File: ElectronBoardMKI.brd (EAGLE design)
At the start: 95.9 x 82.6 mm, 22 parts

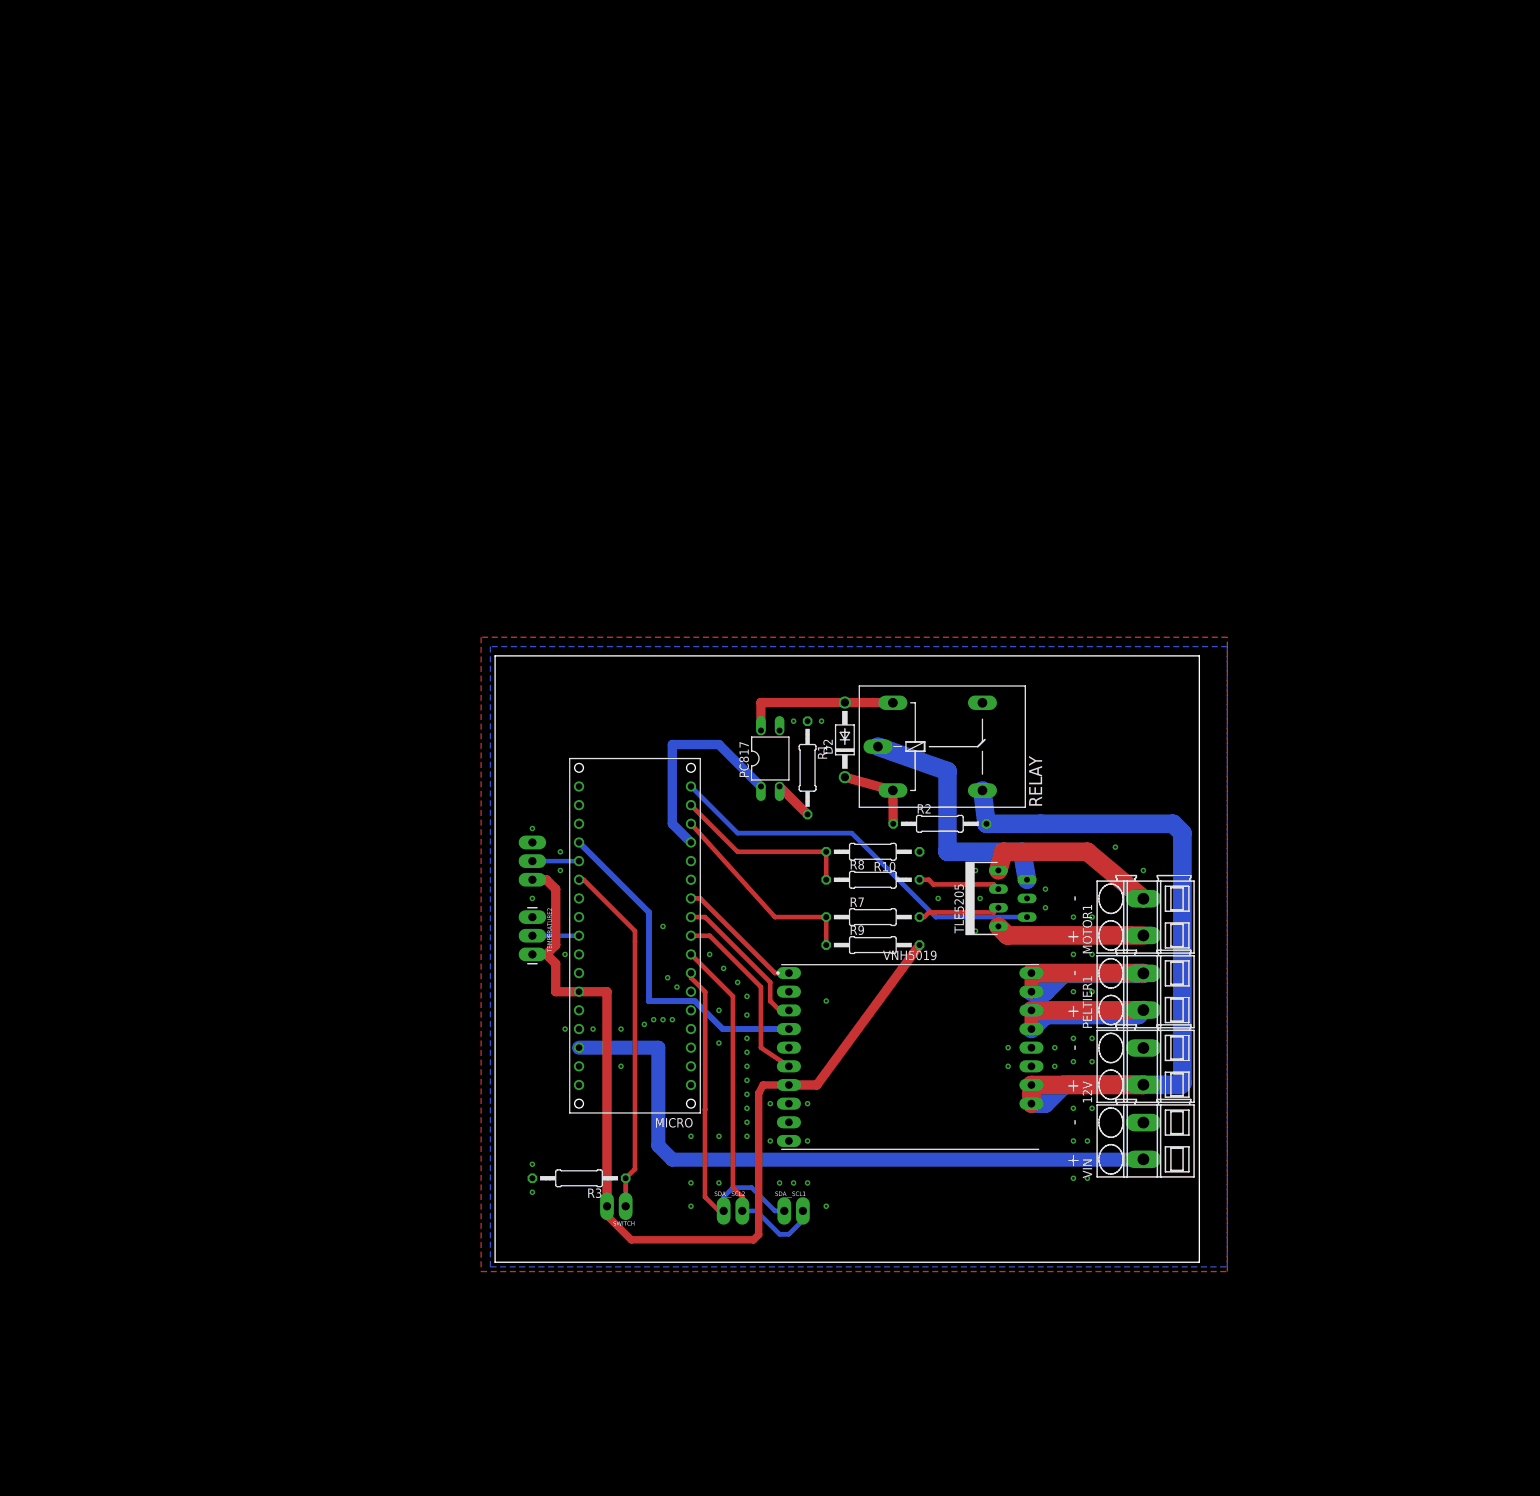
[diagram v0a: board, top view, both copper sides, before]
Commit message: Updated PCB VIAS +more
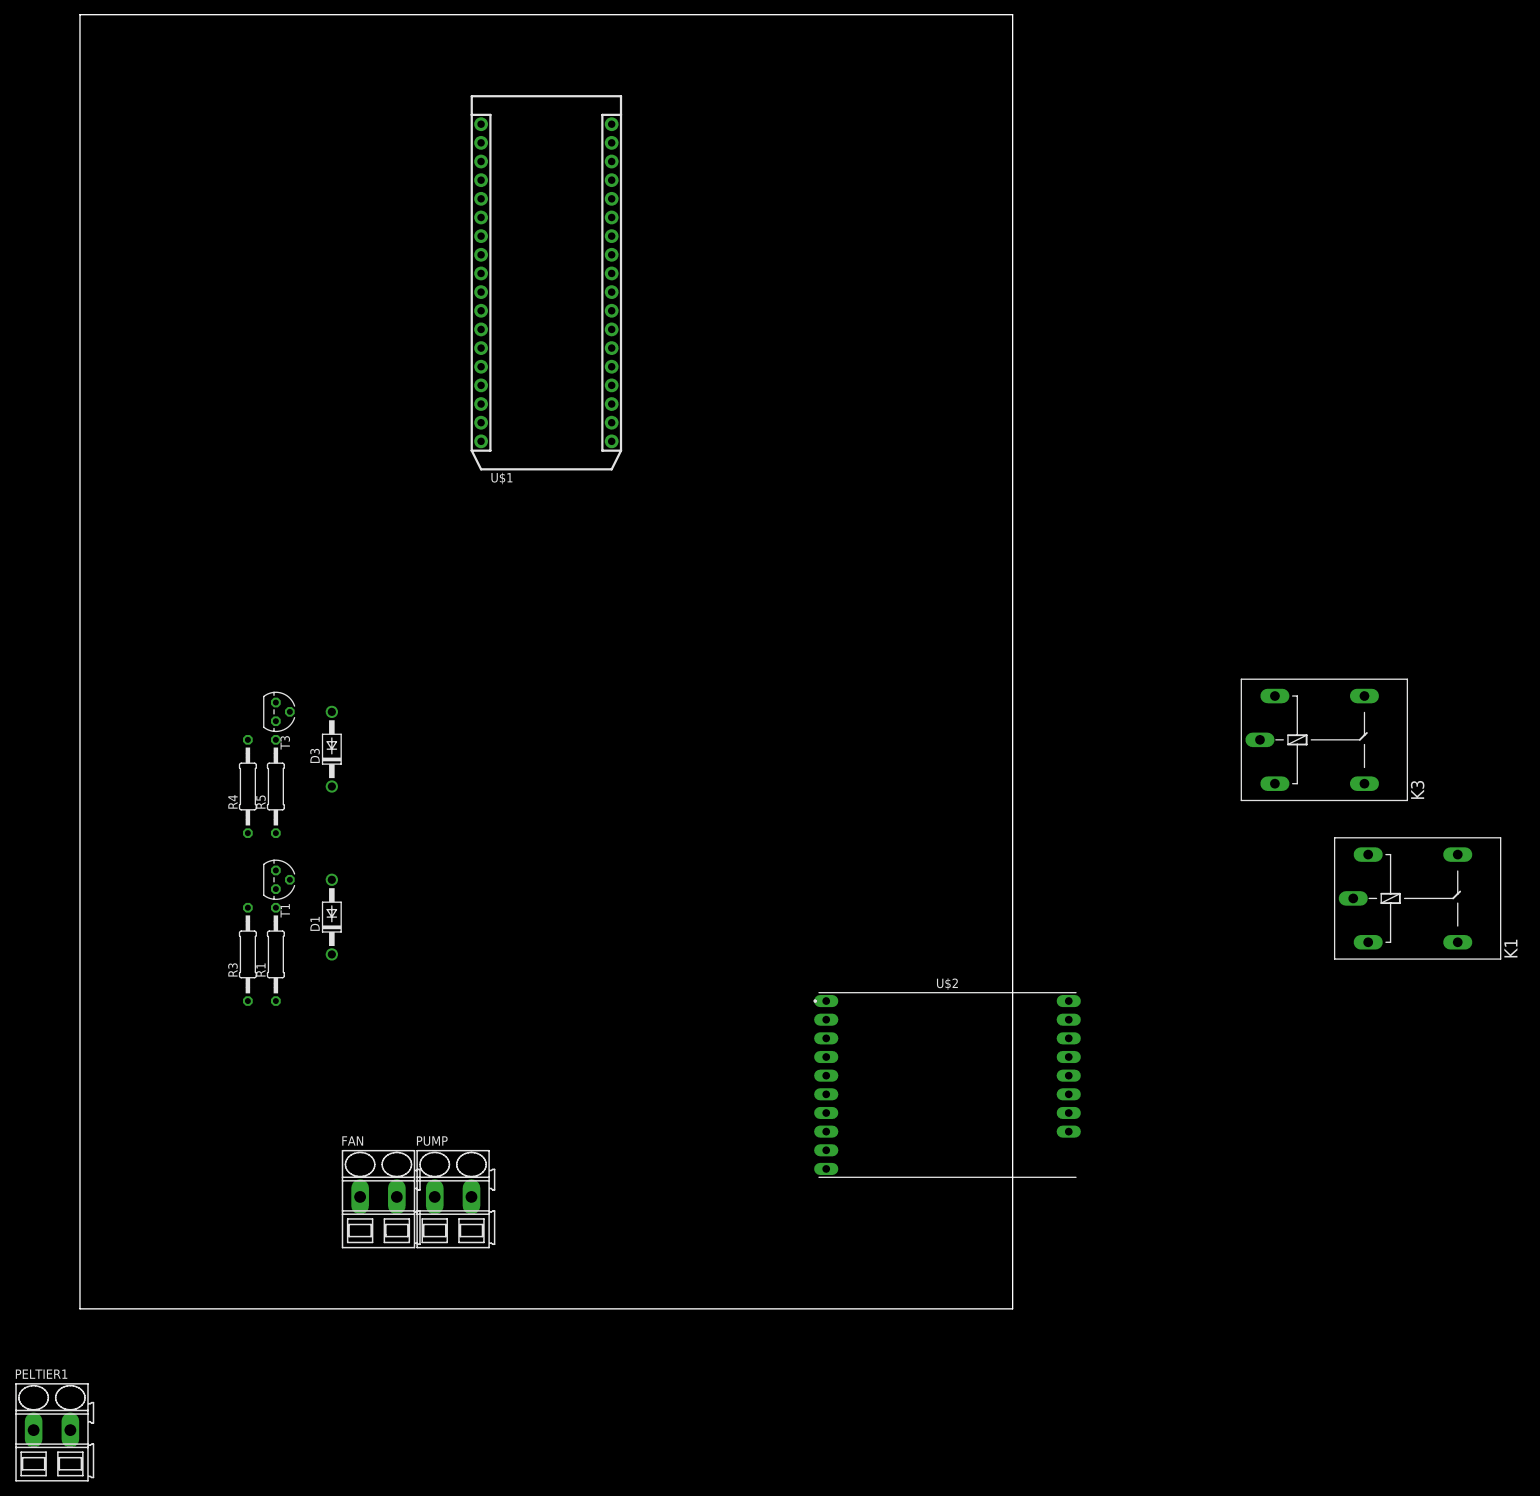
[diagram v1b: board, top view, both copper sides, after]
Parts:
- removed 12V, MOTOR1, VIN: SMKDSP_1,5/2, con-phoenix-smkdsp:SMKDSP_1,5/2
- removed D2: 1N4004, diode:DO41-10
- removed MICRO: ARDUINO_MICROFOOTPRINT, arduino-micro:ARDUINO-MICRO
- removed PC817: PC817, optocoupler:DIL04
- removed R10, R9: 47k, resistor:0207/12
- removed R2: 220, resistor:0207/12
- removed R7, R8: 1k, resistor:0207/12
- removed RELAY: G5LE, relay:G5LE
- removed SDA__SCL1, SDA__SCL2, SWITCH: (no value), SparkFun-Connectors:1X02_LONGPADS
- removed TEMPERATURE1, TEMPERATURE2: (no value), SparkFun-Connectors:1X03_LONGPADS
- removed TLE5205: TLE5205-2, infineon:P-TO220-7-11
- removed VNH5019: VNH5019VNH5019BOARD, GEMS:DIP3302W60P254L2400H500Q20B
- added D1, D3: 1N4004, diode:DO41-10
- added FAN, PUMP: SMKDSP_1,5/2, con-phoenix-smkdsp:SMKDSP_1,5/2
- added K1, K3: G5LE, relay:G5LE
- added R4, R5: (no value), resistor:0207/12
- added T1, T3: 2N3704, transistor:TO92
- added U$1: ELECTRON_WITH_HEADERS, Particle-Devices:ELECTRON
- added U$2: VNH5019VNH5019BOARD, GEMS:DIP3302W60P254L2400H500Q20B
- R1: value 220 -> (none)
- R3: value 4.7k -> (none)
- moved PELTIER1 160.1 mm to (-3.81, -16.5), turned to 0 degrees
- moved R1 76.7 mm to (26.7, 48.3), turned to 90 degrees
- moved R3 54.4 mm to (22.9, 48.3), turned to 90 degrees
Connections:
- removed net +5V: MICRO.5V, R9.2, SWITCH.2, TEMPERATURE1.3, TEMPERATURE2.3, VNH5019.VDD
- removed net DOORSWITCH: MICRO.A2, R3.1, SWITCH.1
- removed net MOTOR-ENABLE: MICRO.D9, PC817.1
- removed net MOTOR-ERRORFLAG: MICRO.D12, TLE5205.2
- removed net MOTOR-IN1: MICRO.D10, R7.1, R9.1
- removed net MOTOR-IN2: MICRO.D11, R10.2, R8.1
- removed net N$10: R7.2, TLE5205.3
- removed net N$13: R8.2, TLE5205.5
- removed net N$14: VNH5019.ENA
- removed net N$18: VNH5019.ENB
- removed net N$21: MICRO.D7
- removed net N$22: MICRO.D8
- removed net N$3: D2.A, PC817.4, RELAY.2
- removed net N$4: RELAY.P, TLE5205.6
- removed net N$6: MOTOR1.1, TLE5205.1
- removed net N$7: MOTOR1.2, TLE5205.7
- removed net PELTIER-CURRENT: MICRO.A0, VNH5019.CS
- removed net PELTIER-INA: MICRO.D6, VNH5019.INA
- removed net PELTIER-INB: MICRO.D4, VNH5019.INB
- removed net PELTIER-PWM: MICRO.D5, VNH5019.PWM
- removed net SCL: MICRO.D3, SDA__SCL1.2, SDA__SCL2.2
- removed net SDA: MICRO.D2, SDA__SCL1.1, SDA__SCL2.1
- removed net TEMPERATURE1: MICRO.A1, TEMPERATURE1.2
- removed net TEMPERATURE2: MICRO.A5, TEMPERATURE2.2
- new net C0: U$1.19
- new net COOLING-CURRENT: U$2.CS
- new net COOLING-INA: U$2.INA
- new net COOLING-INB: U$2.INB
- new net COOLING-PWM: U$2.PWM
- new net N$11: K3.P, PUMP.1
- new net N$12: R4.2, R5.2, T3.1
- new net N$2: D1.A, K1.2, T1.2
- new net N$23: U$1.25
- new net N$24: U$1.26
- new net N$25: U$1.27
- new net N$26: U$1.28
- new net N$27: U$1.18
- new net N$28: U$1.17
- new net N$29: U$1.16
- new net N$30: U$1.15
- new net N$9: D3.A, K3.2, T3.2
- new net SCREEN-BLUE: U$1.22
- new net SCREEN-GREEN: U$1.21
- new net SCREEN-RED: U$1.20
- new net SCREEN-SCL: U$1.24
- new net SCREEN-SDA: U$1.23
- new net SOUND: U$1.5
- new net VBAT: U$1.34
- new net VDD: U$1.36, U$2.VDD
- net +12V: now also D1.C, D3.C, K1.1, K1.S, K3.1, K3.S, U$2.VIN1, U$2.VIN2; no longer 12V.1, R2.2, RELAY.S, VNH5019.VIN1, VNH5019.VIN2
- net GND: now also FAN.2, PUMP.2, R3.1, R4.1, T1.3, T3.3, U$1.2, U$1.33, U$2.GND1, U$2.GND2, U$2.GND3, U$2.GND4; no longer 12V.2, MICRO.GND, MICRO.GND1, PC817.3, R1.1, R10.1, R3.2, TEMPERATURE1.1, TEMPERATURE2.1, TLE5205.4, VIN.2, VNH5019.GND1, VNH5019.GND2, VNH5019.GND3, VNH5019.GND4
- net N$1: now also R3.2, T1.1; no longer PC817.2
- net N$16: now also PELTIER1.2, U$2.OUTB1, U$2.OUTB2; no longer PELTIER1.1, VNH5019.OUTB1, VNH5019.OUTB2
- net N$17: now also PELTIER1.1, U$2.OUTA1, U$2.OUTA2; no longer PELTIER1.2, VNH5019.OUTA1, VNH5019.OUTA2
- net N$5: now also FAN.1, K1.P; no longer D2.C, R2.1, RELAY.1
- net VIN: now also U$1.1; no longer MICRO.VIN, VIN.1
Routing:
- net +5V: track 131.9 -> 0.00 mm
- net +12V: track 105.3 -> 0.00 mm
- net VIN: track 91.0 -> 0.00 mm
- net MOTOR-ERRORFLAG: track 53.1 -> 0.00 mm
- net SCL: track 49.4 -> 0.00 mm
- net DOORSWITCH: track 48.5 -> 0.00 mm
- net SDA: track 46.6 -> 0.00 mm
- net PELTIER-CURRENT: track 46.2 -> 0.00 mm
- net N$4: track 35.0 -> 0.00 mm
- net N$16: track 34.1 -> 0.00 mm
- net N$17: track 34.1 -> 0.00 mm
- net MOTOR-ENABLE: track 28.8 -> 0.00 mm
- net MOTOR-IN1: track 27.9 -> 0.00 mm
- net PELTIER-INB: track 25.3 -> 0.00 mm
- net MOTOR-IN2: track 24.9 -> 0.00 mm
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- removed copper zone on layer 1, net GND
- removed copper zone on layer 16, net GND
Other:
- board size 95.9 x 82.6 mm -> 127 x 176.2 mm
- board text removed: "+"
- board text removed: "-"
